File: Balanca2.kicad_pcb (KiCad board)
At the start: 2 copper layers, 88 x 87.7 mm, 39 parts, among them J1 Conn_01x03_Pin, J2 Conn_01x03_Pin, J3 Conn_01x03_Pin, J4 Conn_01x03_Pin, J5 Conn_01x03_Pin, J6 Conn_01x03, J7 Conn_01x05, Q1 BC547, Q2 BC557, U1 TL084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

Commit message: Mudança da placa v2
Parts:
- removed JP1: Jumper_2_Bridged, TestPoint:TestPoint_Bridge_Pitch5.08mm_Drill0.7mm
- removed R10: 100k, Resistor_THT:R_Axial_DIN0207_L6.3mm_D2.5mm_P2.54mm_Vertical
- removed R11: 100k, Resistor_THT:R_Axial_DIN0204_L3.6mm_D1.6mm_P2.54mm_Vertical
- removed R5, R7: 33k, Resistor_THT:R_Axial_DIN0207_L6.3mm_D2.5mm_P2.54mm_Vertical
- removed R6: 330, Resistor_THT:R_Axial_DIN0207_L6.3mm_D2.5mm_P10.16mm_Horizontal
- removed R8: 10k, Resistor_THT:R_Axial_DIN0207_L6.3mm_D2.5mm_P10.16mm_Horizontal
- removed R9: 10k, Resistor_THT:R_Axial_DIN0207_L6.3mm_D2.5mm_P15.24mm_Horizontal
- removed U3: TL082, Package_DIP:DIP-8_W7.62mm
- added U2: INA128, Package_DIP:DIP-8_W7.62mm, F.Cu at (180.1, 44.3)
- added U8: LM393, Package_DIP:DIP-8_W7.62mm, F.Cu at (203.9, 72.0)
- RV3: value 10k -> 50k
- U1: value TL084 -> TL082; footprint Package_DIP:DIP-14_W7.62mm -> Package_DIP:DIP-8_W7.62mm
- moved JP6 60.4 mm to (174.5, 60.5)
- moved RV3 56.9 mm to (174.3, 38.2), turned to 90 degrees
- moved J4 55.8 mm to (238.0, 29.0)
- moved JP5 55.0 mm to (174.5, 67.5), turned to 180 degrees
- moved U5 53.4 mm to (244.5, 95.1), turned to 90 degrees
- moved D1 48.6 mm to (248.5, 78.0)
- moved J5 44.3 mm to (177.5, 97.5), turned to 90 degrees
- moved C5 44.2 mm to (230.0, 98.0), turned to 90 degrees
- moved R4 43.0 mm to (194.3, 29.0), turned to 0 degrees
- moved U4 42.7 mm to (242.6, 78.0)
- moved D2 41.2 mm to (234.5, 77.8)
- moved J6 40.1 mm to (180.1, 62.0)
- moved J1 40.0 mm to (237.5, 103.5), turned to 90 degrees
- moved C4 37.1 mm to (240.0, 68.7), turned to 0 degrees
- moved J7 32.6 mm to (187.7, 54.0), turned to 180 degrees
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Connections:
- J6 pad 1: /CelulaCargaAlimentacaoV+ -> GND
- J6 pad 3: GND -> /CelulaCargaAlimentacaoV+
- RV3 pad 2: Net-(U1B--) -> Net-(RV3-Pad2)
- RV3 pad 3: Net-(U1B--) -> Net-(RV3-Pad2)
- U1 pad 1: Net-(R5-Pad1) -> unconnected-(U1-Pad1)
- U1 pad 2: Net-(U1A--) -> unconnected-(U1A---Pad2)
- U1 pad 3: /SinalSaida+ -> unconnected-(U1A-+-Pad3)
- U1 pad 4: +15V -> -15V
- U1 pad 5: /SinalSaida- -> AC
- U1 pad 6: Net-(U1B--) -> /CelulaCargaAlimentacaoV+
- U1 pad 7: Net-(R7-Pad2) -> Net-(Q1-B)
- U1 pad 8: /SaidaPrimeiroEstagio -> +15V
- U6 pad 10: GND -> /SaidaPrimeiroEstagio
- U6 pad 8: /SaidaPrimeiroEstagio -> GND
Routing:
- net Net-(U7B-+): track 52.4 -> 106.9 mm, vias 0 -> 2
- net +5V: track 30.9 -> 81.8 mm
- net Net-(R5-Pad1): track 39.6 -> 0.00 mm, vias 2 -> 0
- net /SaidaBalanca: track 26.6 -> 65.2 mm, vias 2 -> 1
- net /SaidaPrimeiroEstagio: track 104.7 -> 137.3 mm, vias 2 -> 0
- net Net-(U1C-+): track 29.2 -> 0.00 mm
- net /V_Offset: track 40.5 -> 14.0 mm
- net AC: track 43.8 -> 18.3 mm
- net /Controle2: track 20.8 -> 41.8 mm
- net GND: track 6.82 -> 27.0 mm
- net -5V: track 53.2 -> 70.7 mm
- net -15V: track 133.1 -> 116.6 mm
- net /Controle1: track 35.4 -> 19.8 mm
- net /CelulaCargaAlimentacaoV+: track 110.6 -> 95.4 mm, vias 5 -> 2
- net Net-(U1A--): track 14.0 -> 0.00 mm
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
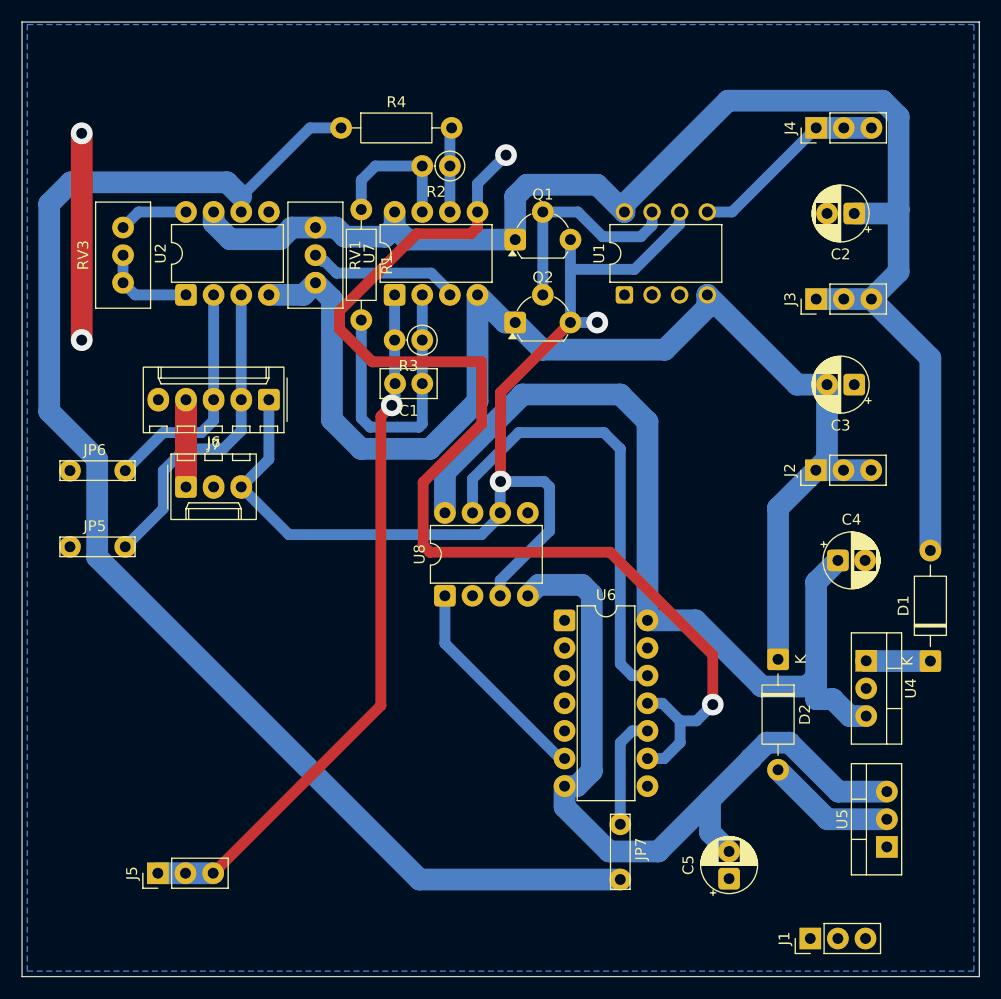
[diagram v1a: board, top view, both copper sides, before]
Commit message: Atualizacao de esquematico da placa 3
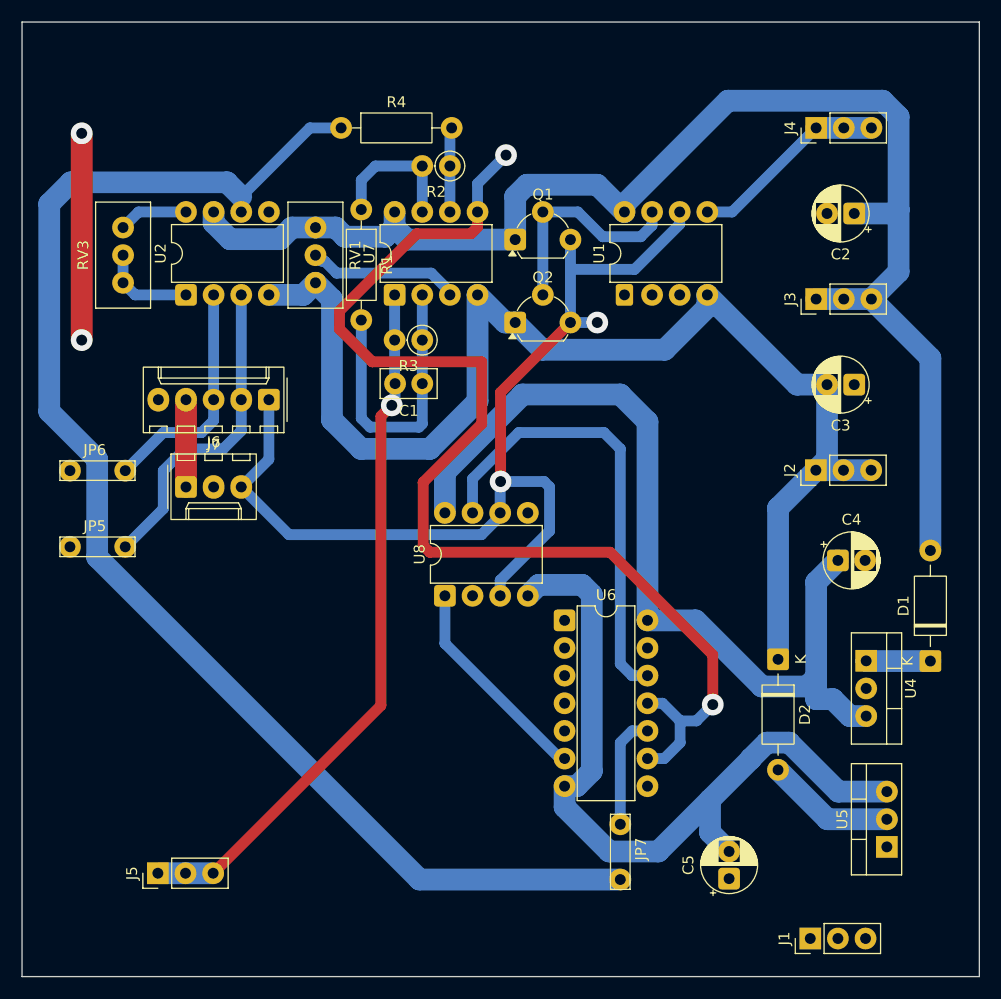
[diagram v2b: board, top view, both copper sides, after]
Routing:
- removed copper zone on B.Cu, net GND
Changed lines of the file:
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@@
 		(pad "1" thru_hole roundrect
 			(at 0 0 90)
-			(size 1.6 1.6)
+			(size 2 1.6)
 			(drill 1)
 			(layers "*.Cu" "*.Mask")
@@
 		(pad "2" thru_hole circle
 			(at 0 2.54 90)
-			(size 1.6 1.6)
+			(size 2 1.6)
 			(drill 1)
 			(layers "*.Cu" "*.Mask")
@@
 		(pad "3" thru_hole circle
 			(at 0 5.08 90)
-			(size 1.6 1.6)
+			(size 2 1.6)
 			(drill 1)
 			(layers "*.Cu" "*.Mask")
@@
 		(pad "4" thru_hole circle
 			(at 0 7.62 90)
-			(size 1.6 1.6)
+			(size 2 1.6)
 			(drill 1)
 			(layers "*.Cu" "*.Mask")
@@
 		(pad "5" thru_hole circle
 			(at 7.62 7.62 90)
-			(size 1.6 1.6)
+			(size 2 1.6)
 			(drill 1)
 			(layers "*.Cu" "*.Mask")
@@
 		(pad "6" thru_hole circle
 			(at 7.62 5.08 90)
-			(size 1.6 1.6)
+			(size 2 1.6)
 			(drill 1)
 			(layers "*.Cu" "*.Mask")
@@
 		(pad "7" thru_hole circle
 			(at 7.62 2.54 90)
-			(size 1.6 1.6)
+			(size 2 1.6)
 			(drill 1)
 			(layers "*.Cu" "*.Mask")
@@
 		(pad "8" thru_hole circle
 			(at 7.62 0 90)
-			(size 1.6 1.6)
+			(size 2 1.6)
 			(drill 1)
 			(layers "*.Cu" "*.Mask")
@@
 		(pad "3" thru_hole oval
 			(at 5.08 0 180)
-			(size 2 2.19)
+			(size 2 2)
 			(drill 1)
 			(layers "*.Cu" "*.Mask")
@@
 		(net "Net-(U7B-+)")
 	)
-	(zone
-		(net "GND")
-		(layer "B.Cu")
-		(name "GND")
-		(hatch edge 0.5)
-		(connect_pads
-			(clearance 0.5)
-		)
-		(min_thickness 0.25)
-		(fill yes
-			(thermal_gap 0.5)
-			(thermal_bridge_width 0.5)
-			(island_removal_mode 1)
-		)
-		(polygon
-			(pts
-				(xy 165.5 19.5) (xy 252.5 19.5) (xy 252.5 106.5) (xy 165.5 106.5)
-			)
-		)
-	)
 	(embedded_fonts no)

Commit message: Inicio do Roteamento
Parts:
- added C1: 470n, Capacitor_THT:C_Disc_D5.0mm_W2.5mm_P2.50mm, F.Cu at (333.0, 56.7)
- added C10: 100n, Capacitor_THT:C_Disc_D5.0mm_W2.5mm_P2.50mm, F.Cu at (339.5, 60.8)
- added C11: 100n, Capacitor_THT:C_Disc_D5.0mm_W2.5mm_P2.50mm, F.Cu at (339.5, 64.8)
- added C12: 100n, Capacitor_THT:C_Disc_D5.0mm_W2.5mm_P2.50mm, F.Cu at (339.5, 68.9)
- added C13: 100n, Capacitor_THT:C_Disc_D5.0mm_W2.5mm_P2.50mm, F.Cu at (346.1, 56.7)
- added C14: 100n, Capacitor_THT:C_Disc_D5.0mm_W2.5mm_P2.50mm, F.Cu at (346.1, 60.8)
- added C15: 100n, Capacitor_THT:C_Disc_D5.0mm_W2.5mm_P2.50mm, F.Cu at (346.1, 64.8)
- added C16: 33p, Capacitor_THT:C_Disc_D5.0mm_W2.5mm_P2.50mm, F.Cu at (346.1, 68.9)
- added C17: 4,7u, Capacitor_THT:CP_Radial_D5.0mm_P2.50mm, F.Cu at (313.1, 72.5)
- added C2: 1u, Capacitor_THT:CP_Radial_D5.0mm_P2.50mm, F.Cu at (313.1, 46.3)
- added C3: 1u, Capacitor_THT:CP_Radial_D5.0mm_P2.50mm, F.Cu at (313.1, 52.8)
- added C4: C_Polarized, Capacitor_THT:CP_Radial_D5.0mm_P2.50mm, F.Cu at (313.1, 59.4)
- added C5: C_Polarized, Capacitor_THT:CP_Radial_D5.0mm_P2.50mm, F.Cu at (313.1, 65.9)
- added C6: 100n, Capacitor_THT:C_Disc_D5.0mm_W2.5mm_P2.50mm, F.Cu at (333.0, 60.8)
- added C7: 100n, Capacitor_THT:C_Disc_D5.0mm_W2.5mm_P2.50mm, F.Cu at (333.0, 64.8)
- added C8: 100n, Capacitor_THT:C_Disc_D5.0mm_W2.5mm_P2.50mm, F.Cu at (333.0, 68.9)
- added C9: 100n, Capacitor_THT:C_Disc_D5.0mm_W2.5mm_P2.50mm, F.Cu at (339.5, 56.7)
- added D3: 1N4007, Diode_THT:D_DO-41_SOD81_P10.16mm_Horizontal, F.Cu at (332.8, 73.0)
- added D4: 1N4007, Diode_THT:D_DO-41_SOD81_P10.16mm_Horizontal, F.Cu at (332.8, 77.3)
- added R10: 100k, Resistor_THT:R_Axial_DIN0207_L6.3mm_D2.5mm_P2.54mm_Vertical, F.Cu at (319.7, 73.4)
- added R11: 100k, Resistor_THT:R_Axial_DIN0207_L6.3mm_D2.5mm_P2.54mm_Vertical, F.Cu at (319.7, 77.4)
- added R12: 10k, Resistor_THT:R_Axial_DIN0207_L6.3mm_D2.5mm_P10.16mm_Horizontal, F.Cu at (319.2, 65.3)
- added R3: 47k, Resistor_THT:R_Axial_DIN0207_L6.3mm_D2.5mm_P2.54mm_Vertical, F.Cu at (319.7, 69.3)
- added R5: 10k, Resistor_THT:R_Axial_DIN0207_L6.3mm_D2.5mm_P10.16mm_Horizontal, F.Cu at (319.2, 45.0)
- added R6: 10k, Resistor_THT:R_Axial_DIN0207_L6.3mm_D2.5mm_P10.16mm_Horizontal, F.Cu at (319.2, 49.1)
- added R7: 330, Resistor_THT:R_Axial_DIN0207_L6.3mm_D2.5mm_P10.16mm_Horizontal, F.Cu at (319.2, 53.1)
- added R8: 330, Resistor_THT:R_Axial_DIN0207_L6.3mm_D2.5mm_P10.16mm_Horizontal, F.Cu at (319.2, 57.2)
- added R9: 33, Resistor_THT:R_Axial_DIN0207_L6.3mm_D2.5mm_P10.16mm_Horizontal, F.Cu at (319.2, 61.2)
- added U1: TL082, Package_DIP:DIP-8_W7.62mm, F.Cu at (332.5, 45.0)
- added U7: TL082, Package_DIP:DIP-8_W7.62mm, F.Cu at (343.3, 45.0)
- RV3: value 50k -> 10K
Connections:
- J2 pad 1: -15V -> /Entrada-15V
- J2 pad 2: -15V -> /Entrada-15V
- J2 pad 3: -15V -> /Entrada-15V
- J3 pad 1: +15V -> /Entrada+15V
- J3 pad 2: +15V -> /Entrada+15V
- J3 pad 3: +15V -> /Entrada+15V
- Q1 pad 1: +15V -> Net-(Q1-C)
- Q1 pad 3: /CelulaCargaAlimentacaoV+ -> Net-(Q1-E)
- Q2 pad 1: -15V -> Net-(Q2-C)
- Q2 pad 3: /CelulaCargaAlimentacaoV+ -> Net-(Q1-E)
- R1 pad 2: Net-(U7A--) -> Net-(C17-Pad1)
- RV1 pad 1: -15V -> Net-(R10-Pad2)
- RV1 pad 3: +15V -> Net-(R11-Pad1)
- U2 pad 1: Net-(RV3-Pad2) -> Net-(RV3-Pad1)
- U2 pad 8: Net-(RV3-Pad1) -> Net-(RV3-Pad2)
- U4 pad 1: Net-(D1-K) -> +15V
- U5 pad 2: Net-(D2-A) -> -15V
- U6 pad 1: unconnected-(U6-Pad1) -> GND
- U6 pad 13: GND -> -5V
- U6 pad 2: unconnected-(U6-Pad2) -> GND
- U6 pad 3: unconnected-(U6-Pad3) -> GND
- U6 pad 4: unconnected-(U6-Pad4) -> GND
- U6 pad 5: unconnected-(U6-Pad5) -> -5V
- U8 pad 8: +5V -> +15V
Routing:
- net /SaidaPrimeiroEstagio: track 137.3 -> 0.00 mm
- net +15V: track 130.8 -> 0.00 mm
- net -15V: track 116.6 -> 0.00 mm
- net Net-(U7B-+): track 106.9 -> 0.00 mm, vias 2 -> 0
- net /CelulaCargaAlimentacaoV+: track 95.4 -> 0.00 mm, vias 2 -> 0
- net +5V: track 81.8 -> 0.00 mm
- net -5V: track 70.7 -> 0.00 mm
- net /SaidaBalanca: track 65.2 -> 4.16 mm, vias 1 -> 0
- net /Controle2: track 41.8 -> 0.00 mm
- net /SinalSaida+: track 29.6 -> 0.00 mm
- net GND: track 27.0 -> 0.00 mm, vias 2 -> 0
- net Net-(U7A--): track 27.0 -> 4.16 mm
- net /SinalSaida-: track 21.6 -> 0.00 mm
- net Net-(Q1-B): track 20.3 -> 0.00 mm
- net /Controle1: track 19.8 -> 0.00 mm
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
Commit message: Atualizacao de footprints
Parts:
- removed the C1 at (201.8, 52.5)
- removed the C1 at (333.0, 56.7)
- removed the C2 at (241.5, 36.9)
- removed the C2 at (313.1, 46.3)
- removed the C3 at (313.1, 52.8)
- removed the C3 at (241.5, 52.6)
- removed the C4 at (240.0, 68.7)
- removed the C4 at (313.1, 59.4)
- removed the C5 at (313.1, 65.9)
- removed the C5 at (230.0, 98.0)
- removed D1, D2: 1N4007, Diode_THT:D_DO-41_SOD81_P10.16mm_Horizontal
- removed the R3 at (319.7, 69.3)
- removed the R3 at (201.8, 48.5)
- removed the U1 at (332.5, 45.0)
- removed the U1 at (220.4, 44.3)
- removed the U7 at (343.3, 45.0)
- removed the U7 at (199.3, 44.3)
- added C1: 470n, Capacitor_THT:C_Disc_D5.0mm_W2.5mm_P2.50mm, F.Cu at (127.5, 53.2)
- added C2: 1u, Capacitor_THT:CP_Radial_D5.0mm_P2.50mm, F.Cu at (169.0, 53.5)
- added C3: 1u, Capacitor_THT:CP_Radial_D5.0mm_P2.50mm, F.Cu at (169.0, 60.0)
- added C4: C_Polarized, Capacitor_THT:CP_Radial_D5.0mm_P2.50mm, F.Cu at (169.0, 66.6)
- added C5: C_Polarized, Capacitor_THT:CP_Radial_D5.0mm_P2.50mm, F.Cu at (169.0, 73.2)
- added R3: 47k, Resistor_THT:R_Axial_DIN0207_L6.3mm_D2.5mm_P2.54mm_Vertical, F.Cu at (147.1, 57.3)
- added U1: TL082, Package_DIP:DIP-8_W7.62mm, F.Cu at (212.5, 95.6)
- added U7: TL082, Package_DIP:DIP-8_W7.62mm, F.Cu at (192.4, 43.4)
- R5: footprint Resistor_THT:R_Axial_DIN0207_L6.3mm_D2.5mm_P10.16mm_Horizontal -> Resistor_THT:R_Axial_DIN0204_L3.6mm_D1.6mm_P5.08mm_Vertical
- moved R12 212.8 mm to (107.1, 81.6)
- moved C10 205.5 mm to (134.0, 57.3)
- moved C11 205.5 mm to (134.0, 61.3)
- moved C12 205.5 mm to (134.0, 65.4)
- moved C13 205.5 mm to (140.6, 53.2)
- moved C14 205.5 mm to (140.6, 57.3)
- moved C15 205.5 mm to (140.6, 61.3)
- moved C9 205.5 mm to (134.0, 53.2)
- moved C8 205.5 mm to (127.5, 65.4)
- moved C17 192.4 mm to (120.9, 80.7)
- moved R10 173.0 mm to (147.1, 61.3)
- moved R11 173.0 mm to (147.1, 65.4)
- moved D3 163.5 mm to (169.6, 83.2)
- moved D4 163.5 mm to (169.6, 87.5)
- moved C16 149.6 mm to (208.7, 128.1)
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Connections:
- net Net-(Q1-B) renamed /SaídaBuffer
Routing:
- net +5V: track 0.00 -> 19.4 mm
- net /V_Offset: track 14.5 -> 0.00 mm
- net /SaidaPrimeiroEstagio: track 0.00 -> 11.4 mm
- net Net-(RV3-Pad2): track 0.00 -> 8.63 mm
- net Net-(U7B-+): track 0.00 -> 8.56 mm
- net Net-(RV3-Pad1): track 0.00 -> 5.80 mm
- net /SaidaDemodulada: track 4.23 -> 0.00 mm
- net Net-(U7A--): track 4.16 -> 0.00 mm
- net /SaidaBalanca: track 4.16 -> 0.00 mm
- net /Controle1: track 0.00 -> 3.88 mm
- net /Controle2: track 0.00 -> 3.50 mm
- net -15V: track 0.00 -> 3.00 mm
- net +15V: track 0.00 -> 2.88 mm

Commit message: Inicio do novo Roteamento
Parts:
- moved C10 116.5 mm to (248.4, 79.4)
- moved C11 104.2 mm to (235.0, 87.0), turned to 180 degrees
- moved R4 102.8 mm to (201.7, 45.2), turned to 90 degrees
- moved C14 95.1 mm to (235.3, 49.2), turned to 90 degrees
- moved C15 94.0 mm to (230.2, 33.0), turned to 180 degrees
- moved C8 93.0 mm to (218.6, 47.0)
- moved J1 92.7 mm to (264.1, 44.1)
- moved J2 92.7 mm to (264.1, 34.6)
- moved J3 92.7 mm to (264.1, 25.1)
- moved U4 92.7 mm to (262.6, 94.7)
- moved U5 92.7 mm to (262.6, 100.7)
- moved C2 92.7 mm to (261.7, 53.5)
- moved C3 92.7 mm to (261.7, 60.0)
- moved C4 92.7 mm to (261.7, 66.6)
- moved C5 92.7 mm to (261.7, 73.2)
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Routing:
- net -5V: track 0.00 -> 34.4 mm
- net /Controle1: track 3.88 -> 36.4 mm
- net /SaidaDemodulada: track 0.00 -> 21.7 mm
- net /V_Offset: track 0.00 -> 17.8 mm
- net Net-(U7B-+): track 8.56 -> 21.9 mm
- net Net-(C17-Pad1): track 0.00 -> 12.4 mm
- net Net-(U7B--): track 0.00 -> 11.1 mm
- net /SaidaPrimeiroEstagio: track 11.4 -> 21.4 mm
- net +5V: track 19.4 -> 10.3 mm
- net +15V: track 2.88 -> 11.8 mm
- net /SinalSaida-: track 0.00 -> 8.00 mm
- net /SinalSaida+: track 0.00 -> 8.00 mm
- net /SaidaBalanca: track 0.00 -> 7.65 mm
- net /CelulaCargaAlimentacaoV+: track 0.00 -> 7.50 mm
- net Net-(U7A--): track 0.00 -> 7.38 mm
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
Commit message: Roteamento iniciado, falta verificar erros
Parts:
- R10, R11: footprint Resistor_THT:R_Axial_DIN0207_L6.3mm_D2.5mm_P2.54mm_Vertical -> Resistor_THT:R_Axial_DIN0207_L6.3mm_D2.5mm_P10.16mm_Horizontal
- R8: footprint Resistor_THT:R_Axial_DIN0207_L6.3mm_D2.5mm_P10.16mm_Horizontal -> Resistor_THT:R_Axial_DIN0207_L6.3mm_D2.5mm_P5.08mm_Vertical
- moved J4 105.2 mm to (239.1, 30.6), turned to 180 degrees
- moved D3 100.2 mm to (171.6, 40.7), turned to 90 degrees
- moved JP7 95.2 mm to (198.9, 66.9)
- moved JP5 89.3 mm to (195.1, 101.2), turned to 90 degrees
- moved J3 88.9 mm to (175.4, 30.6), turned to 180 degrees
- moved JP6 87.9 mm to (195.1, 91.2), turned to 90 degrees
- moved C2 87.0 mm to (175.7, 40.7)
- moved U5 84.7 mm to (200.7, 42.9), turned to 180 degrees
- moved C5 79.0 mm to (188.4, 43.8)
- moved D4 74.6 mm to (214.2, 30.6), turned to -90 degrees
- moved J1 68.8 mm to (196.7, 30.6), turned to 180 degrees
- moved J2 46.4 mm to (217.9, 30.6), turned to 180 degrees
- moved C3 45.7 mm to (220.3, 40.7), turned to 180 degrees
- moved U4 43.2 mm to (240.4, 57.6), turned to -90 degrees
- moved Q2 41.3 mm to (233.9, 81.7), turned to 90 degrees
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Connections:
- R10 pad 1: -15V -> Net-(R10-Pad1)
- R10 pad 2: Net-(R10-Pad2) -> +15V
- R11 pad 1: Net-(R11-Pad1) -> -15V
- R11 pad 2: +15V -> Net-(R11-Pad2)
- RV1 pad 1: Net-(R10-Pad2) -> Net-(R10-Pad1)
- RV1 pad 3: Net-(R11-Pad1) -> Net-(R11-Pad2)
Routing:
- net -15V: track 9.57 -> 244.2 mm, vias 0 -> 4
- net +15V: track 11.8 -> 232.8 mm, vias 0 -> 2
- net AC: track 0.00 -> 80.5 mm
- net Net-(Q1-E): track 0.00 -> 44.6 mm
- net /CelulaCargaAlimentacaoV+: track 7.50 -> 45.0 mm, vias 0 -> 2
- net +5V: track 10.3 -> 45.7 mm, vias 0 -> 2
- net /SaidaBalanca: track 7.65 -> 31.2 mm
- net -5V: track 34.4 -> 57.6 mm, vias 0 -> 1
- net /Controle2: track 7.00 -> 27.3 mm
- net /SaídaBuffer: track 0.00 -> 19.7 mm
- net /SinalSaida+: track 8.00 -> 24.9 mm
- net /SinalSaida-: track 8.00 -> 21.0 mm
- net /Entrada+15V: track 0.00 -> 8.95 mm
- net /Entrada-15V: track 0.00 -> 8.81 mm
- net /Controle1: track 36.4 -> 44.0 mm
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- added copper zone on B.Cu, net GND

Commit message: Alteracoes de footprint e melhorias de trilhas
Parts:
- removed C4: C_Polarized, Capacitor_THT:CP_Radial_D5.0mm_P2.50mm
- removed C8: 100n, Capacitor_THT:C_Disc_D5.0mm_W2.5mm_P2.50mm
- removed JP7: Jumper_2_Bridged, TestPoint:TestPoint_Bridge_Pitch5.08mm_Drill0.7mm
- added C18: 100n, Capacitor_THT:C_Disc_D5.0mm_W2.5mm_P2.50mm, F.Cu at (210.8, 70.0)
- added JP10: Jumper_2_Bridged, Library:TestPoint_Bridge_Pitch7.62mm_Drill1.3mm, F.Cu at (199.0, 67.5)
- added JP8: Jumper_2_Bridged, Library:TestPoint_Bridge_Pitch6.35mm_Drill1.3mm, F.Cu at (225.8, 71.2)
- added JP9: Jumper_2_Bridged, Library:TestPoint_Bridge_Pitch5.08mm_Drill1.3mm, F.Cu at (241.1, 62.5)
- R10, R11, R7: footprint Resistor_THT:R_Axial_DIN0207_L6.3mm_D2.5mm_P10.16mm_Horizontal -> Resistor_THT:R_Axial_DIN0207_L6.3mm_D2.5mm_P15.24mm_Horizontal
- moved J4 43.0 mm to (241.4, 73.5), turned to 90 degrees
- moved U4 23.4 mm to (220.5, 70.0), turned to 180 degrees
- moved C14 15.6 mm to (247.0, 62.5), turned to 180 degrees
- moved J5 15.5 mm to (184.9, 97.6), turned to 180 degrees
- moved JP5 5.53 mm to (190.9, 97.5), turned to 0 degrees
- moved R11 5.49 mm to (172.8, 76.7)
- moved JP6 4.60 mm to (190.9, 93.2), turned to 0 degrees
- moved R5 4.41 mm to (213.3, 65.0)
- moved C10 1.50 mm to (217.1, 75.3)
- moved C11 1.50 mm to (228.3, 86.2)
- moved C16 1.50 mm to (216.0, 100.9)
- moved C6 1.50 mm to (214.4, 85.4)
- moved J6 1.50 mm to (205.7, 98.4)
- moved J7 1.50 mm to (210.8, 90.9)
- moved Q1 1.50 mm to (242.5, 83.3)
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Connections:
- R4 pad 1: /SaidaPrimeiroEstagio -> /SaidaPrimeiroEstagioA
- U8 pad 3: /CelulaCargaAlimentacaoV+ -> Net-(JP8-B)
- U8 pad 6: /CelulaCargaAlimentacaoV+ -> Net-(JP8-B)
- U8 pad 8: +15V -> Net-(JP9-B)
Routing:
- net AC: track 80.5 -> 18.9 mm
- net +15V: track 232.8 -> 198.3 mm, vias 2 -> 0
- net Net-(JP8-B): track 0.00 -> 31.5 mm
- net +5V: track 45.7 -> 19.2 mm, vias 2 -> 0
- net /CelulaCargaAlimentacaoV+: track 45.0 -> 20.5 mm, vias 2 -> 0
- net -15V: track 244.2 -> 230.9 mm
- net /SaidaBalanca: track 31.2 -> 38.8 mm
- net /SinalSaida+: track 24.9 -> 30.6 mm
- net /SaidaPrimeiroEstagio: track 19.2 -> 14.2 mm
- net /Controle2: track 27.3 -> 22.9 mm
- net /SinalSaida-: track 21.0 -> 24.5 mm
- net /SaidaPrimeiroEstagioA: track 0.00 -> 3.45 mm
- net Net-(JP9-B): track 0.00 -> 3.45 mm
- net /V_Offset: track 17.8 -> 19.3 mm

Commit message: Finalizada Versao 3
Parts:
- JP8: footprint Library:TestPoint_Bridge_Pitch6.35mm_Drill1.3mm -> Library:TestPoint_Bridge_Pitch7.62mm_Drill1.3mm
- R10, R11: footprint Resistor_THT:R_Axial_DIN0207_L6.3mm_D2.5mm_P15.24mm_Horizontal -> Resistor_THT:R_Axial_DIN0207_L6.3mm_D2.5mm_P10.16mm_Horizontal
- moved R10 5.41 mm to (182.9, 82.0)
- moved RV1 3.31 mm to (188.9, 82.0)
- moved C5 2.60 mm to (188.4, 41.1)
- moved JP8 1.31 mm to (225.8, 72.5), turned to 76 degrees
- moved R11 0.20 mm to (172.8, 76.9)
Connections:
- JP8 pad 2: Net-(JP8-B) -> /CelulaCargaAlimentacaoV+
- U8 pad 3: Net-(JP8-B) -> /CelulaCargaAlimentacaoV+
- U8 pad 6: Net-(JP8-B) -> /CelulaCargaAlimentacaoV+
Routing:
- net /CelulaCargaAlimentacaoV+: track 20.5 -> 110.9 mm, vias 0 -> 2
- net Net-(JP8-B): track 31.5 -> 0.00 mm
- net GND: track 6.24 -> 32.6 mm, vias 2 -> 8
- net +15V: track 198.3 -> 218.7 mm, vias 0 -> 1
- net -15V: track 230.9 -> 222.4 mm, vias 4 -> 2
- net /SaidaBalanca: track 38.8 -> 42.4 mm
- net Net-(R10-Pad1): track 3.92 -> 6.02 mm
- net Net-(R11-Pad2): track 4.34 -> 6.02 mm
- net Net-(Q1-E): track 44.6 -> 45.3 mm
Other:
- outline, holes or cut-outs redrawn
